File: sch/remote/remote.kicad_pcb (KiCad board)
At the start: 2 copper layers, 24 parts, among them J1 swd, J2 power_sw, J3 USB_A, Q1 DTD114E, U1 STM32F103C8Tx_usb, U2 XC6206-33, U3 TSOP17xx, Y1 8M

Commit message: 0402 caps
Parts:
- C1, C2, C3, C5, C6, C7, C8, C9: footprint Capacitor_SMD:C_0805_2012Metric -> Capacitor_SMD:C_0402_1005Metric
- moved C7 18.3 mm to (154.5, 55.6)
- moved C5 17.3 mm to (170.8, 51.7), turned to 270 degrees
- moved D1 7.06 mm to (175.1, 56.4), turned to 270 degrees
- moved C11 5.38 mm to (174.3, 51.2), turned to 90 degrees
- moved U3 2.55 mm to (172.7, 56.6)
- moved J2 2.54 mm to (174.8, 61.0)
- moved Q1 1.83 mm to (166.7, 61.4)
- moved C4 1.77 mm to (157.1, 60.2)
- moved C3 1.40 mm to (170.8, 53.7), turned to 90 degrees
- moved C1 1.40 mm to (170.8, 57.6), turned to 90 degrees
- moved C2 1.40 mm to (170.8, 55.7), turned to 270 degrees
- moved C6 1.00 mm to (154.5, 49.8)
- moved C8 0.90 mm to (154.5, 62.5)
- moved J1 0.85 mm to (161.3, 61.7)
- moved R2 0.69 mm to (154.5, 54.5)
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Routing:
- net +3V3: track 117.8 -> 104.5 mm
- net +5V: track 32.3 -> 41.3 mm
- net GND: track 134.1 -> 137.6 mm
- net /PWR: track 7.49 -> 4.95 mm
- net Net-(J2-Pad3): track 4.07 -> 2.30 mm
- net /IR: track 12.9 -> 11.1 mm
- net Net-(C10-Pad1): track 7.50 -> 9.13 mm
- net Net-(J3-Pad2): track 5.28 -> 4.35 mm
- net Net-(C3-Pad2): track 6.27 -> 5.56 mm
- net /SWCLK: track 5.11 -> 4.39 mm
- net /DP: track 6.10 -> 5.42 mm
- net Net-(C2-Pad1): track 7.02 -> 6.38 mm
- net Net-(C1-Pad1): track 9.96 -> 9.34 mm
- net Net-(D1-Pad2): track 3.06 -> 2.52 mm
- net Net-(J3-Pad3): track 4.49 -> 4.99 mm

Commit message: loger desc, new pcb for remote
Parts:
- C10, C4, C8, D1, R4, U2: moved to B.Cu
- J2: footprint Connector_PinHeader_2.54mm:PinHeader_1x03_P2.54mm_Horizontal -> Connector_PinHeader_2.54mm:PinHeader_1x03_P2.54mm_Vertical
- moved D1 21.9 mm to (153.3, 54.4), turned to 90 degrees
- moved U2 5.86 mm to (159.7, 60.1), turned to 270 degrees
- moved J1 4.75 mm to (156.9, 59.9), turned to 180 degrees
- moved Q1 4.23 mm to (162.6, 60.3)
- moved C4 4.08 mm to (159.7, 57.1), turned to 180 degrees
- moved C8 3.77 mm to (157.5, 60.2), turned to 90 degrees
- moved J2 3.37 mm to (171.4, 60.7)
- moved R4 3.34 mm to (153.2, 58.9), turned to 0 degrees
- moved C10 1.79 mm to (156.0, 60.3), turned to 90 degrees
- moved J3 1.52 mm to (142.2, 55.1)
- moved C11 1.10 mm to (173.8, 52.1)
- moved C7 1.05 mm to (155.3, 56.2), turned to 90 degrees
- moved C6 0.99 mm to (155.1, 49.1), turned to 90 degrees
- moved U3 0.59 mm to (172.6, 57.2)
- moved R3 0.23 mm to (154.7, 52.2)
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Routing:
- net +3V3: track 104.5 -> 62.7 mm, vias 0 -> 3
- net +5V: track 41.3 -> 8.04 mm, vias 0 -> 1
- net Net-(D1-Pad2): track 2.52 -> 32.2 mm
- net /SWDIO: track 12.7 -> 7.68 mm
- net GND: track 137.6 -> 134.7 mm, vias 0 -> 1
- net /PWR: track 4.95 -> 2.96 mm
- net /SWCLK: track 4.39 -> 2.82 mm
- net Net-(J3-Pad3): track 4.99 -> 3.75 mm
- net Net-(C10-Pad1): track 9.13 -> 8.19 mm
- net Net-(J2-Pad3): track 2.30 -> 3.02 mm
- net Net-(J3-Pad2): track 4.35 -> 3.69 mm
- added copper zone on B.Cu, net +3V3
- added copper zone on B.Cu, net GND

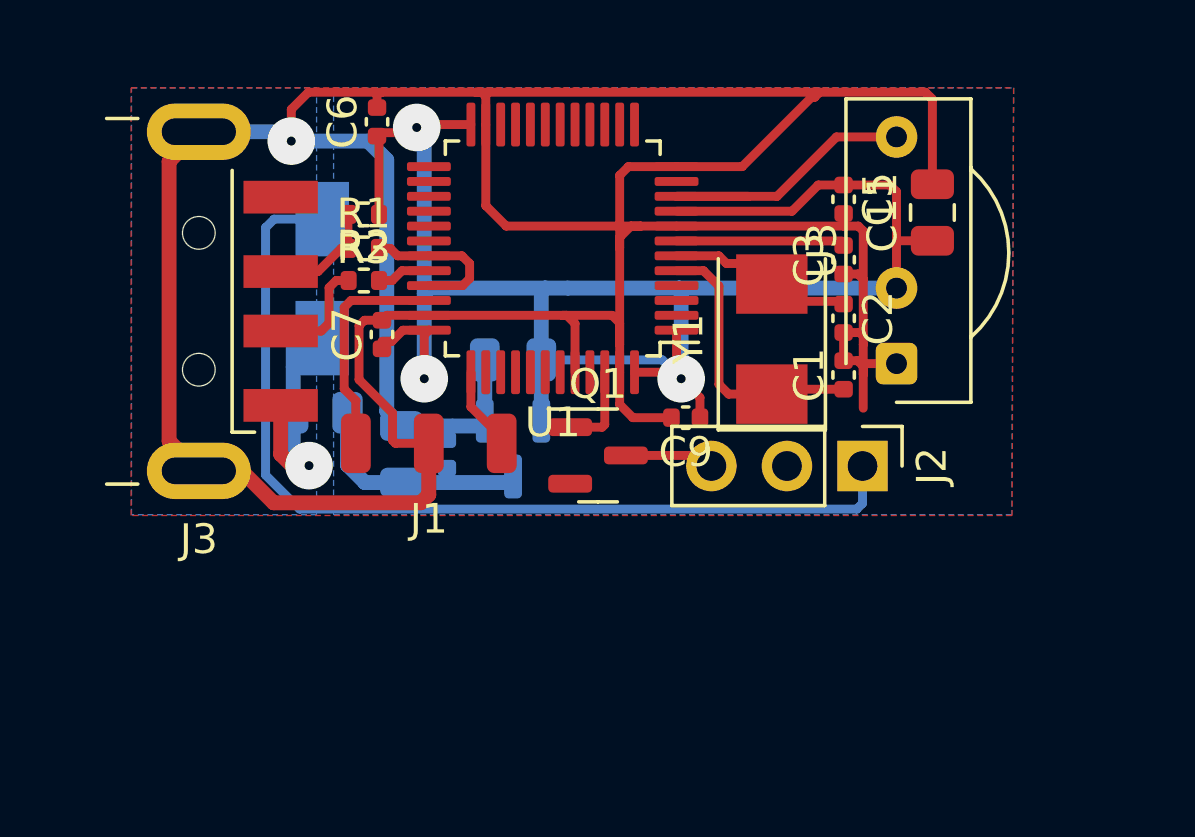
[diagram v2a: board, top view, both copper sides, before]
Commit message: two layer IR, USB CDC almost compl
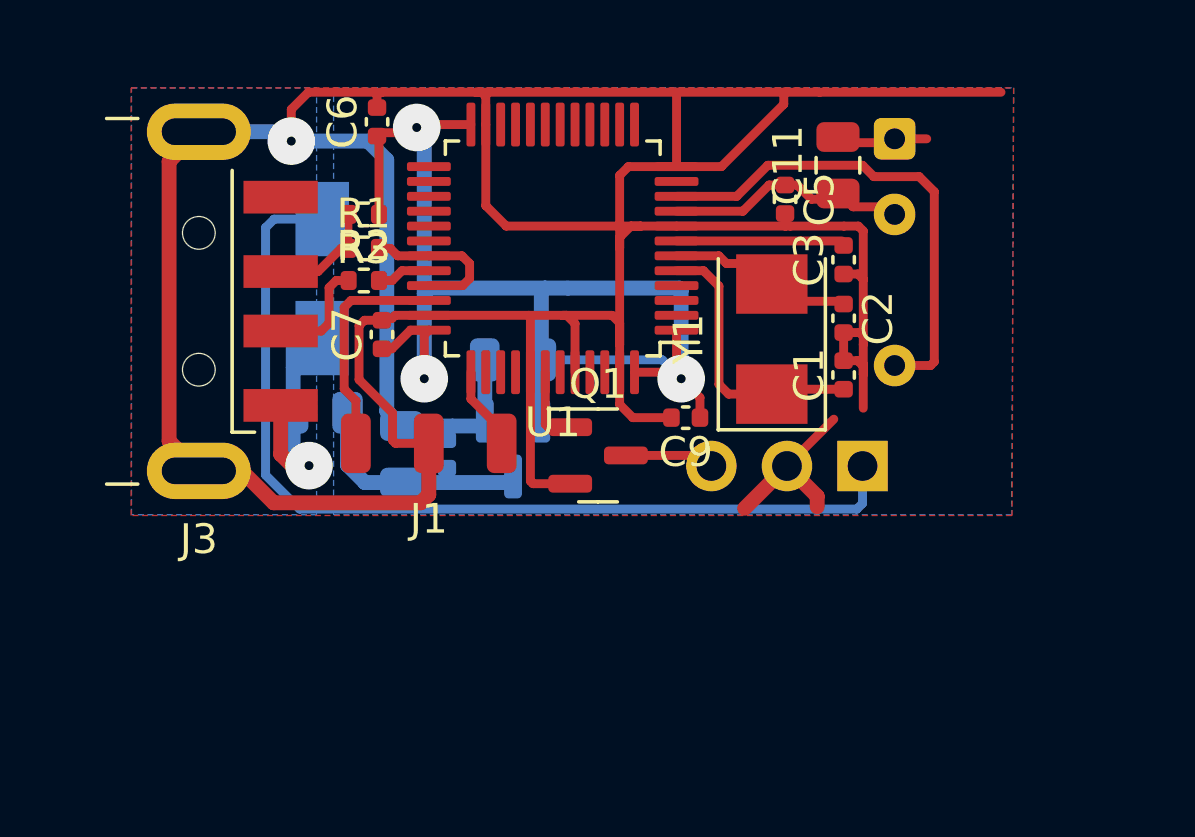
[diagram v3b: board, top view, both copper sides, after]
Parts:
- J2, U3: moved to B.Cu
- moved U3 7.56 mm to (172.5, 49.7), turned to 270 degrees
- moved C11 3.55 mm to (170.6, 50.5)
- moved C5 1.97 mm to (168.8, 51.7)
- turned J2 to 90 degrees
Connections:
- U1 pad 12: GND -> Net-(U1-Pad12)
- U1 pad 41: Net-(U1-Pad41) -> GND
- U1 pad 42: Net-(U1-Pad42) -> /PWR
- U1 pad 45: /SWDIO -> Net-(U1-Pad45)
- U1 pad 46: /PWR -> Net-(U1-Pad46)
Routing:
- net GND: track 134.7 -> 150.5 mm
- net +3V3: track 62.7 -> 51.9 mm
- net /IR: track 10.6 -> 16.6 mm

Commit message: убрался в файлах
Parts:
- U3: value TSOP17xx -> TSOP41xx; footprint OptoDevice:Vishay_CAST-3Pin -> OptoDevice:Vishay_MOLD-3Pin
- moved U3 0.94 mm to (172.8, 50.5)
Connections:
- U3 pad 1: GND -> /IR
- U3 pad 2: +3V3 -> GND
- U3 pad 3: /IR -> +3V3
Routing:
- net /IR: track 16.6 -> 8.08 mm
- net +3V3: track 51.9 -> 58.7 mm
- net GND: track 150.5 -> 148.8 mm
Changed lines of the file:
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@@
     (thickness 1.6)
     (drawings 0)
-    (tracks 236)
+    (tracks 233)
     (zones 0)
     (modules 24)
@@
     (add_net "Net-(U1-Pad46)")
   )
+  (module OptoDevice:Vishay_MOLD-3Pin (layer B.Cu)
+    (at 172.847 50.546 270)
+    (descr "IR Receiver Vishay TSOP-xxxx, MOLD package, see https://www.vishay.com/docs/82669/tsop32s40f.pdf")
+    (tags "IR Receiver Vishay TSOP-xxxx MOLD")
+    (fp_text reference U3 (at 2.5 2.25 270) (layer B.SilkS)
+      (effects (font (size 1 1) (thickness 0.15)) (justify mirror))
+    )
+    (fp_text value TSOP41xx (at 2.5 -5 270) (layer B.Fab)
+      (effects (font (size 1 1) (thickness 0.15)) (justify mirror))
+    )
+    (fp_arc (start 2.64 -1.15) (end 5.14 -2.25) (angle -132) (layer B.Fab) (width 0.1))
+    (fp_arc (start 2.64 -1.2) (end 5.24 -2.3) (angle -134.1358099) (layer B.SilkS) (width 0.12))
+    (fp_text user %R (at 2.675 -1.316 90) (layer B.Fab)
+      (effects (font (size 1 1) (thickness 0.15)) (justify mirror))
+    )
+    (fp_line (start 5.6 -2.2) (end -0.2 -2.2) (layer B.Fab) (width 0.1))
+    (fp_line (start -0.2 -2.2) (end -0.2 0.5) (layer B.Fab) (width 0.1))
+    (fp_line (start 0.55 1.25) (end 5.6 1.25) (layer B.Fab) (width 0.1))
+    (fp_line (start 5.6 1.25) (end 5.6 -2.2) (layer B.Fab) (width 0.1))
+    (fp_line (start 5.7 -2.3) (end 5.7 -1.1) (layer B.SilkS) (width 0.12))
+    (fp_line (start 5.7 -2.3) (end 5.24 -2.3) (layer B.SilkS) (width 0.12))
+    (fp_line (start 5.62 1.36) (end 2.54 1.36) (layer B.SilkS) (width 0.12))
+    (fp_line (start 6.23 -4.13) (end -1.15 -4.13) (layer B.CrtYd) (width 0.05))
+    (fp_line (start 6.23 -4.13) (end 6.23 1.5) (layer B.CrtYd) (width 0.05))
+    (fp_line (start -1.15 1.5) (end -1.15 -4.13) (layer B.CrtYd) (width 0.05))
+    (fp_line (start -1.15 1.5) (end 6.23 1.5) (layer B.CrtYd) (width 0.05))
+    (fp_line (start 0.04 -2.3) (end -0.18 -2.3) (layer B.SilkS) (width 0.12))
+    (fp_line (start 0.55 1.25) (end -0.2 0.5) (layer B.Fab) (width 0.1))
+    (pad 3 thru_hole circle (at 5.08 0 270) (size 1.8 1.8) (drill 0.9) (layers *.Cu *.Mask)
+      (net 5 +3V3))
+    (pad 2 thru_hole circle (at 2.54 0 270) (size 1.8 1.8) (drill 0.9) (layers *.Cu *.Mask)
+      (net 1 GND))
+    (pad 1 thru_hole roundrect (at 0 0 270) (size 1.8 1.8) (drill 0.9) (layers *.Cu *.Mask) (roundrect_rratio 0.138)
+      (net 35 /IR))
+    (model ${KICAD6_3DMODEL_DIR}/OptoDevice.3dshapes/Vishay_MOLD-3Pin.wrl
+      (at (xyz 0 0 0))
+      (scale (xyz 1 1 1))
+      (rotate (xyz 0 0 0))
+    )
+  )
   (module Connector_PinHeader_2.54mm:PinHeader_1x03_P2.54mm_Vertical (layer B.Cu)
     (at 171.45 60.6552 90)
@@
       (net 2 "Net-(C1-Pad1)"))
     (model ${KICAD6_3DMODEL_DIR}/Crystal.3dshapes/Crystal_SMD_0603-2Pin_6.0x3.5mm.wrl
-      (at (xyz 0 0 0))
-      (scale (xyz 1 1 1))
-      (rotate (xyz 0 0 0))
-    )
-  )
-  (module OptoDevice:Vishay_CAST-3Pin (layer B.Cu)
-    (at 172.5295 49.657 270)
-    (descr "IR Receiver Vishay TSOP-xxxx, CAST package, see https://www.vishay.com/docs/82493/tsop311.pdf")
-    (tags "IRReceiverVishayTSOP-xxxx CAST")
-    (fp_text reference U3 (at 3.8 2.5 270) (layer B.SilkS)
-      (effects (font (size 1 1) (thickness 0.15)) (justify mirror))
-    )
-    (fp_text value TSOP17xx (at 3.4 -4.8 90) (layer B.Fab)
-      (effects (font (size 1 1) (thickness 0.15)) (justify mirror))
-    )
-    (fp_line (start 0.9 -2.5) (end 6.6 -2.5) (layer B.SilkS) (width 0.12))
-    (fp_line (start 6.5 -2.5) (end 8.9 -2.5) (layer B.SilkS) (width 0.12))
-    (fp_line (start 8.9 -2.5) (end 8.9 1.7) (layer B.SilkS) (width 0.12))
-    (fp_line (start 8.9 1.7) (end 0 1.7) (layer B.SilkS) (width 0.12))
-    (fp_line (start -1.3 0) (end -1.3 -2.5) (layer B.SilkS) (width 0.12))
-    (fp_line (start -1.3 -2.5) (end 0.9 -2.5) (layer B.SilkS) (width 0.12))
-    (fp_line (start -0.2 1.6) (end 8.8 1.6) (layer B.Fab) (width 0.1))
-    (fp_line (start 8.8 1.6) (end 8.8 -2.4) (layer B.Fab) (width 0.1))
-    (fp_line (start 8.8 -2.4) (end -1.2 -2.4) (layer B.Fab) (width 0.1))
-    (fp_line (start -1.2 -2.4) (end -1.2 0.6) (layer B.Fab) (width 0.1))
-    (fp_line (start -1.45 1.85) (end 9.05 1.85) (layer B.CrtYd) (width 0.05))
-    (fp_line (start -1.45 1.85) (end -1.45 -3.88) (layer B.CrtYd) (width 0.05))
-    (fp_line (start 9.05 -3.88) (end 9.05 1.85) (layer B.CrtYd) (width 0.05))
-    (fp_line (start 9.05 -3.88) (end -1.45 -3.88) (layer B.CrtYd) (width 0.05))
-    (fp_line (start -0.2 1.6) (end -1.2 0.6) (layer B.Fab) (width 0.1))
-    (fp_arc (start 3.72 0.15) (end 6.47 -2.45) (angle -93.5) (layer B.Fab) (width 0.1))
-    (fp_arc (start 3.72 0) (end 6.55 -2.5) (angle -97) (layer B.SilkS) (width 0.12))
-    (fp_text user %R (at 3.8 -1.017 270) (layer B.Fab)
-      (effects (font (size 1 1) (thickness 0.15)) (justify mirror))
-    )
-    (pad 3 thru_hole circle (at 7.62 0 270) (size 1.4 1.4) (drill 0.7) (layers *.Cu *.Mask)
-      (net 35 /IR))
-    (pad 2 thru_hole circle (at 2.54 0 270) (size 1.4 1.4) (drill 0.7) (layers *.Cu *.Mask)
-      (net 5 +3V3))
-    (pad 1 thru_hole roundrect (at 0 0 270) (size 1.4 1.4) (drill 0.7) (layers *.Cu *.Mask) (roundrect_rratio 0.178)
-      (net 1 GND))
-    (model ${KICAD6_3DMODEL_DIR}/OptoDevice.3dshapes/Vishay_CAST-3Pin.wrl
       (at (xyz 0 0 0))
       (scale (xyz 1 1 1))
@@
   (segment (start 171.47501 54.38101) (end 171.295 54.201) (width 0.3) (layer F.Cu) (net 1))
   (segment (start 171.47501 52.75401) (end 171.311 52.59) (width 0.3) (layer F.Cu) (net 1))
-  (segment (start 171.47501 54.38101) (end 171.47501 52.75401) (width 0.3) (layer F.Cu) (net 1))
   (segment (start 170.827 52.59) (end 171.311 52.59) (width 0.3) (layer F.Cu) (net 1))
   (segment (start 171.47501 56.56541) (end 171.47501 56.28601) (width 0.3) (layer F.Cu) (net 1))
@@
   (segment (start 168.8585 52.59) (end 169.025 52.59) (width 0.3) (layer F.Cu) (net 1))
   (segment (start 165.1985 52.59) (end 168.8585 52.59) (width 0.3) (layer F.Cu) (net 1))
-  (segment (start 172.4 49.7865) (end 172.5295 49.657) (width 0.3) (layer F.Cu) (net 1))
-  (segment (start 170.6245 49.7865) (end 172.4 49.7865) (width 0.3) (layer F.Cu) (net 1))
-  (segment (start 172.5295 49.657) (end 173.609 49.657) (width 0.3) (layer F.Cu) (net 1))
   (segment (start 165.1985 50.59) (end 166.707 50.59) (width 0.3) (layer F.Cu) (net 1))
   (segment (start 168.80349 48.49351) (end 168.80349 48.08999) (width 0.3) (layer F.Cu) (net 1))
@@
   (segment (start 160.286 55.638) (end 160.238 55.59) (width 0.3) (layer F.Cu) (net 1))
   (segment (start 156.8735 55.59) (end 160.238 55.59) (width 0.3) (layer F.Cu) (net 1))
+  (segment (start 171.50002 53.086) (end 171.47501 53.11101) (width 0.3) (layer F.Cu) (net 1))
+  (segment (start 171.47501 53.11101) (end 171.47501 52.75401) (width 0.3) (layer F.Cu) (net 1))
+  (segment (start 172.847 53.086) (end 171.50002 53.086) (width 0.3) (layer F.Cu) (net 1))
+  (segment (start 171.47501 54.38101) (end 171.47501 53.11101) (width 0.3) (layer F.Cu) (net 1))
   (segment (start 165.1985 54.09) (end 166.104 54.09) (width 0.3) (layer F.Cu) (net 2))
   (segment (start 166.104 54.09) (end 166.624 54.61) (width 0.3) (layer F.Cu) (net 2))
@@
   (segment (start 167.4295 52.09) (end 168.3105 51.209) (width 0.3) (layer F.Cu) (net 5))
   (segment (start 165.1985 52.09) (end 167.4295 52.09) (width 0.3) (layer F.Cu) (net 5))
-  (segment (start 170.6245 51.6865) (end 170.876 51.6865) (width 0.3) (layer F.Cu) (net 5))
-  (segment (start 170.876 51.6865) (end 171.1325 51.943) (width 0.3) (layer F.Cu) (net 5))
-  (segment (start 172.2755 51.943) (end 172.5295 52.197) (width 0.3) (layer F.Cu) (net 5))
-  (segment (start 171.1325 51.943) (end 172.2755 51.943) (width 0.3) (layer F.Cu) (net 5))
+  (segment (start 170.6245 51.496) (end 170.9445 51.816) (width 0.3) (layer F.Cu) (net 5))
+  (segment (start 170.9445 51.816) (end 174.117 51.816) (width 0.3) (layer F.Cu) (net 5))
+  (segment (start 174.117 51.816) (end 174.371 52.07) (width 0.3) (layer F.Cu) (net 5))
+  (segment (start 174.371 52.07) (end 174.371 55.372) (width 0.3) (layer F.Cu) (net 5))
+  (segment (start 174.117 55.626) (end 172.847 55.626) (width 0.3) (layer F.Cu) (net 5))
+  (segment (start 174.371 55.372) (end 174.117 55.626) (width 0.3) (layer F.Cu) (net 5))
   (segment (start 154.138 60.626) (end 154.138 58.8645) (width 0.5) (layer B.Cu) (net 6))
   (segment (start 154.7235 61.2115) (end 154.138 60.626) (width 0.5) (layer B.Cu) (net 6))
@@
   (segment (start 154.4204 58.4592) (end 154.4204 59.8932) (width 0.3) (layer F.Cu) (net 20))
   (segment (start 154.0256 58.0644) (end 154.4204 58.4592) (width 0.3) (layer F.Cu) (net 20))
-  (segment (start 173.863 57.15) (end 173.736 57.277) (width 0.3) (layer F.Cu) (net 35))
-  (segment (start 173.355 50.927) (end 173.863 51.435) (width 0.3) (layer F.Cu) (net 35))
-  (segment (start 171.45 50.546) (end 171.831 50.927) (width 0.3) (layer F.Cu) (net 35))
   (segment (start 168.26638 50.546) (end 171.45 50.546) (width 0.3) (layer F.Cu) (net 35))
   (segment (start 167.22238 51.59) (end 168.26638 50.546) (width 0.3) (layer F.Cu) (net 35))
   (segment (start 165.1985 51.59) (end 167.22238 51.59) (width 0.3) (layer F.Cu) (net 35))
-  (segment (start 173.863 51.435) (end 173.863 57.15) (width 0.3) (layer F.Cu) (net 35))
-  (segment (start 171.831 50.927) (end 173.355 50.927) (width 0.3) (layer F.Cu) (net 35))
-  (segment (start 173.736 57.277) (end 172.5295 57.277) (width 0.3) (layer F.Cu) (net 35))
+  (segment (start 171.45 50.546) (end 172.847 50.546) (width 0.3) (layer F.Cu) (net 35))
   (zone (net 1) (net_name GND) (layer F.Cu) (hatch edge 0.508)
     (connect_pads (clearance 0.508))
